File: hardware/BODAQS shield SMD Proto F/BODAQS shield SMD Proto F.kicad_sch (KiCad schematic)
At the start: 32 parts, among them J1 Analog1, J2 Analog2, J3 Analog3, J4 Analog4, J5 Bar, J6 I2C1, J7 UART, J8 Navigation, J9 SPI, U2 MCP6004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

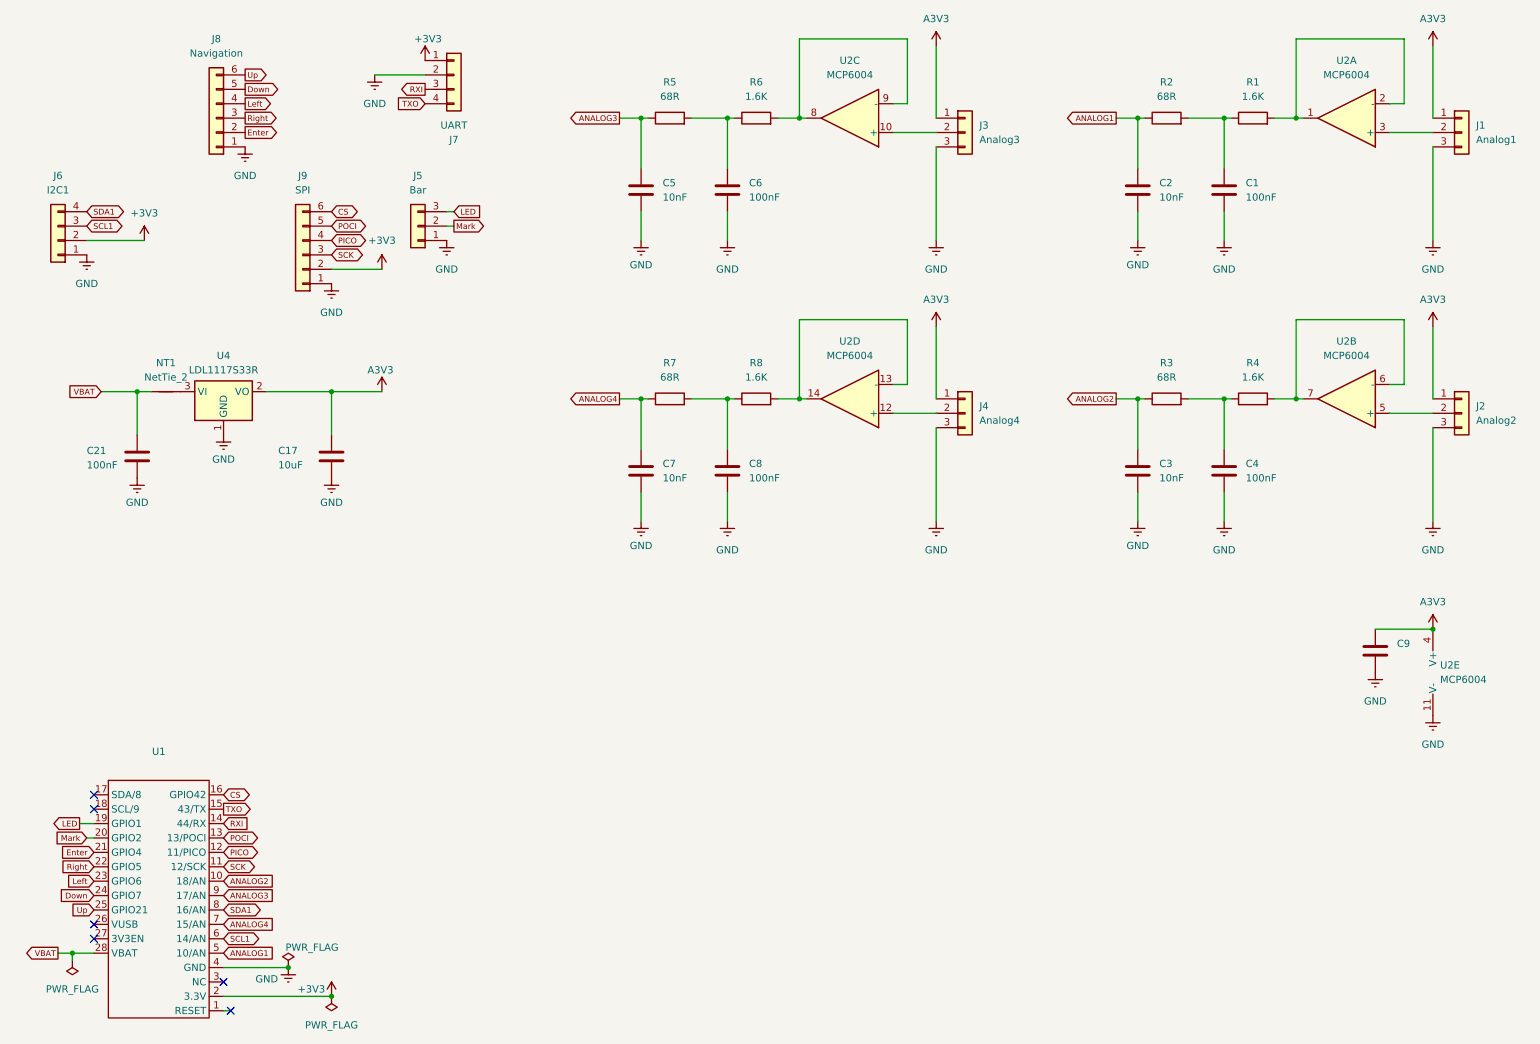
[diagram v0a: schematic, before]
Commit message: Progress in rev F of PCB
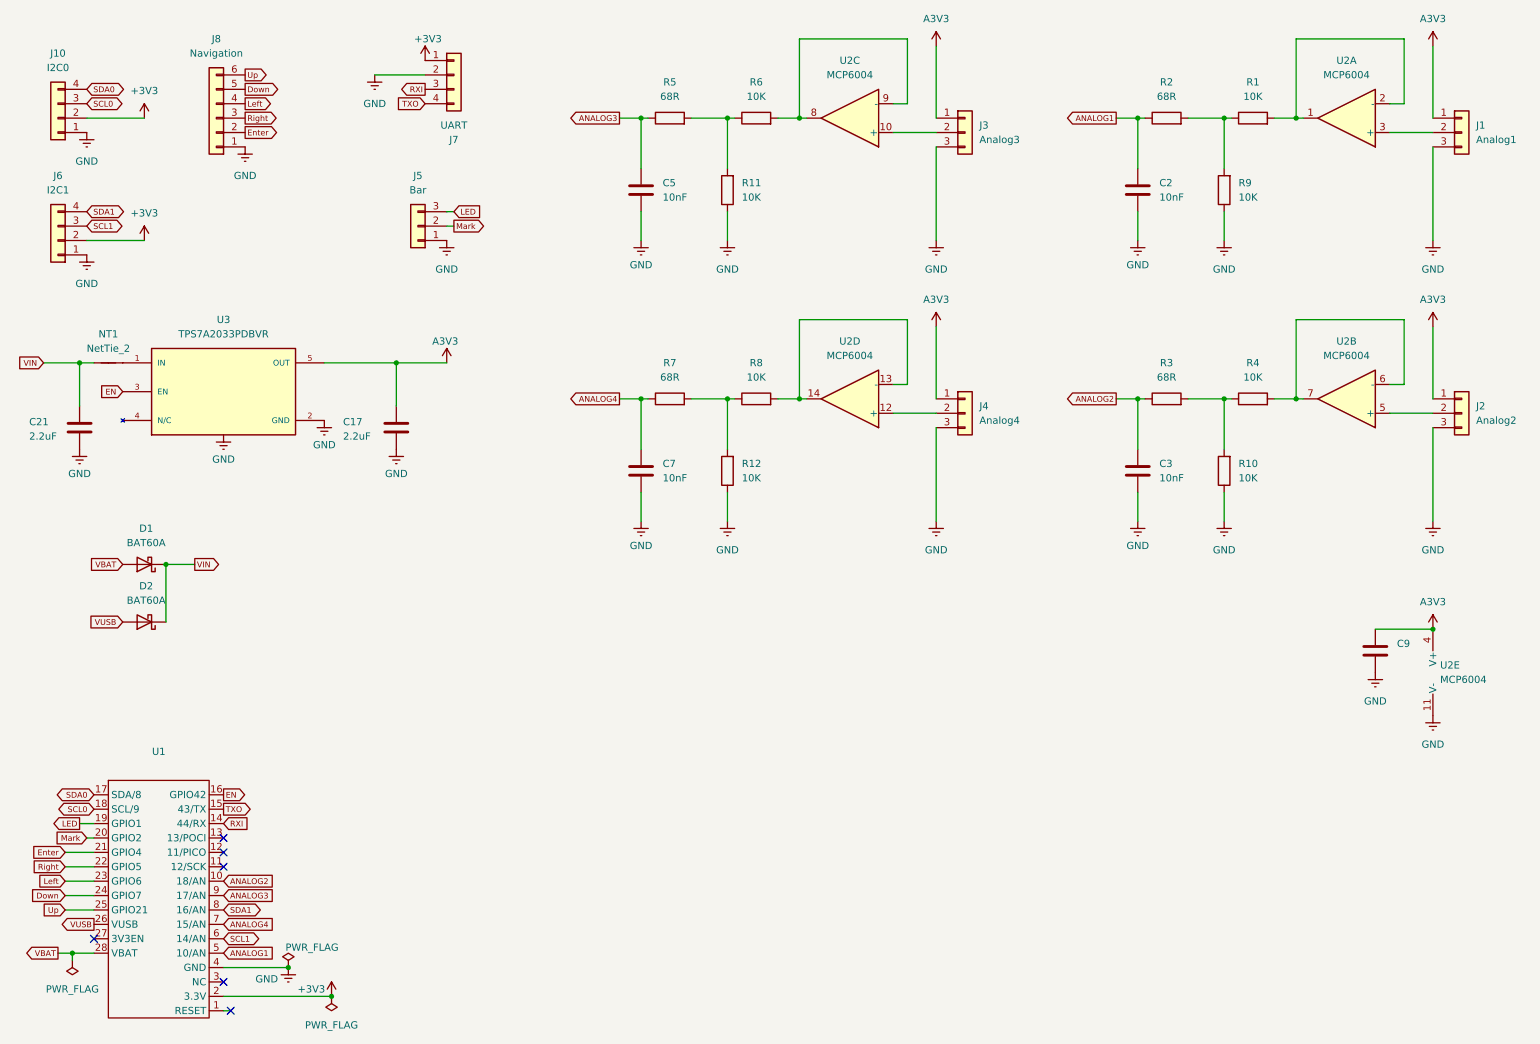
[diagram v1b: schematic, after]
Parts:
- removed C1, C4, C6, C8: 100nF, Capacitor_SMD:C_0603_1608Metric, symbol Device:C
- removed J9: SPI, Connector_PinHeader_2.54mm:PinHeader_1x06_P2.54mm_Vertical, symbol Connector_Generic:Conn_01x06
- removed U4: LDL1117S33R, Package_TO_SOT_SMD:SOT-223-3_TabPin2, symbol Regulator_Linear:LD1117V33
- added D1, D2: BAT60A, Diode_SMD:D_SOD-323, symbol Diode:BAT60A
- added J10: I2C0, Connector_PinHeader_2.00mm:PinHeader_1x04_P2.00mm_Vertical, symbol Connector_Generic:Conn_01x04
- added R10, R11, R12, R9: 10K, Resistor_SMD:R_0603_1608Metric, symbol Device:R
- added U3: TPS7A2033PDBVR, Package_TO_SOT_SMD:SOT-23-5, symbol TPS7A2033PDBVR:TPS7A2033PDBVR
- C17: value 10uF -> 2.2uF
- C21: value 100nF -> 2.2uF
- R1, R4, R6, R8: value 1.6K -> 10K
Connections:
- net +3V3: now also J10.2 (Pin_2)
- net A3V3: now also U3.5 (OUT)
- net GND: now also J10.1 (Pin_1), R10.1, R11.1, R12.1, R9.1, U3.2 (GND)
- net VBAT: now also D1.2 (A); no longer C21.1, NT1.1
- net at R5.2, R6.1: now also R11.2
- net at R7.2, R8.1: now also R12.2
- net at R3.2, R4.1: now also R10.2
- net at NT1.2: now also U3.1 (IN)
- net SDA0: now reaches U1.17 (SDA/8)
- net SDA0: now also J10.4 (Pin_4)
- net SCL0: now reaches U1.18 (SCL/9)
- net SCL0: now also J10.3 (Pin_3)
- net VUSB: now reaches U1.26 (VUSB)
- net VUSB: now also D2.2 (A)
- net at R1.1, R2.2: now also R9.2
- net CS renamed EN
- net EN: now also U3.3 (EN)
- net PICO: no longer names the net of U1.12 (11/PICO)
- net POCI: no longer names the net of U1.13 (13/POCI)
- net SCK: no longer names the net of U1.11 (12/SCK)
- new net VIN: C21.1, D1.1 (K), D2.1 (K), NT1.1
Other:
- moved on the sheet: C17, C21, NT1
